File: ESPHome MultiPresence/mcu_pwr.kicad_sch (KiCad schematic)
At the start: 26 parts, among them J2 USB_C_Receptacle_Power

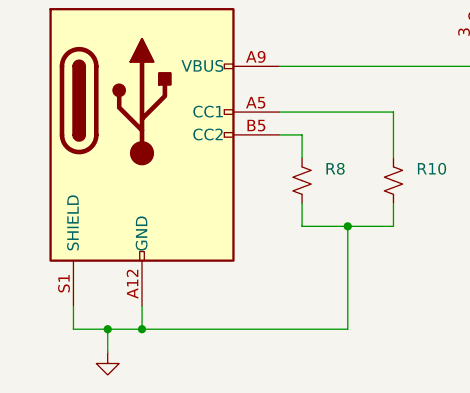
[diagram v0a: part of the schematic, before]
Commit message: small schematic changes
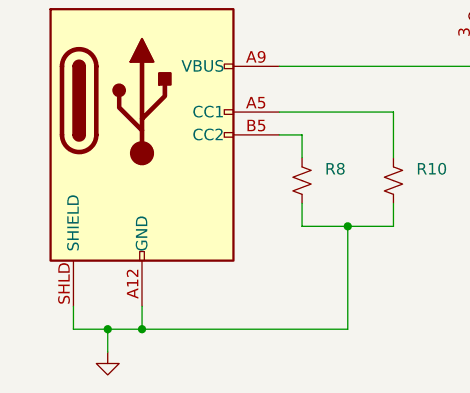
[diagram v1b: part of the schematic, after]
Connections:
- net GND: now also J2.SHLD (SHIELD); no longer J2.S1 (SHIELD)
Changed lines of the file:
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@@
     (pin "B5")
     (pin "B9")
-    (pin "S1")
+    (pin "SHLD")
   )
   (symbol (lib_id "Device:R_Small_US") (at 229.87 90.17 0) (unit 1)

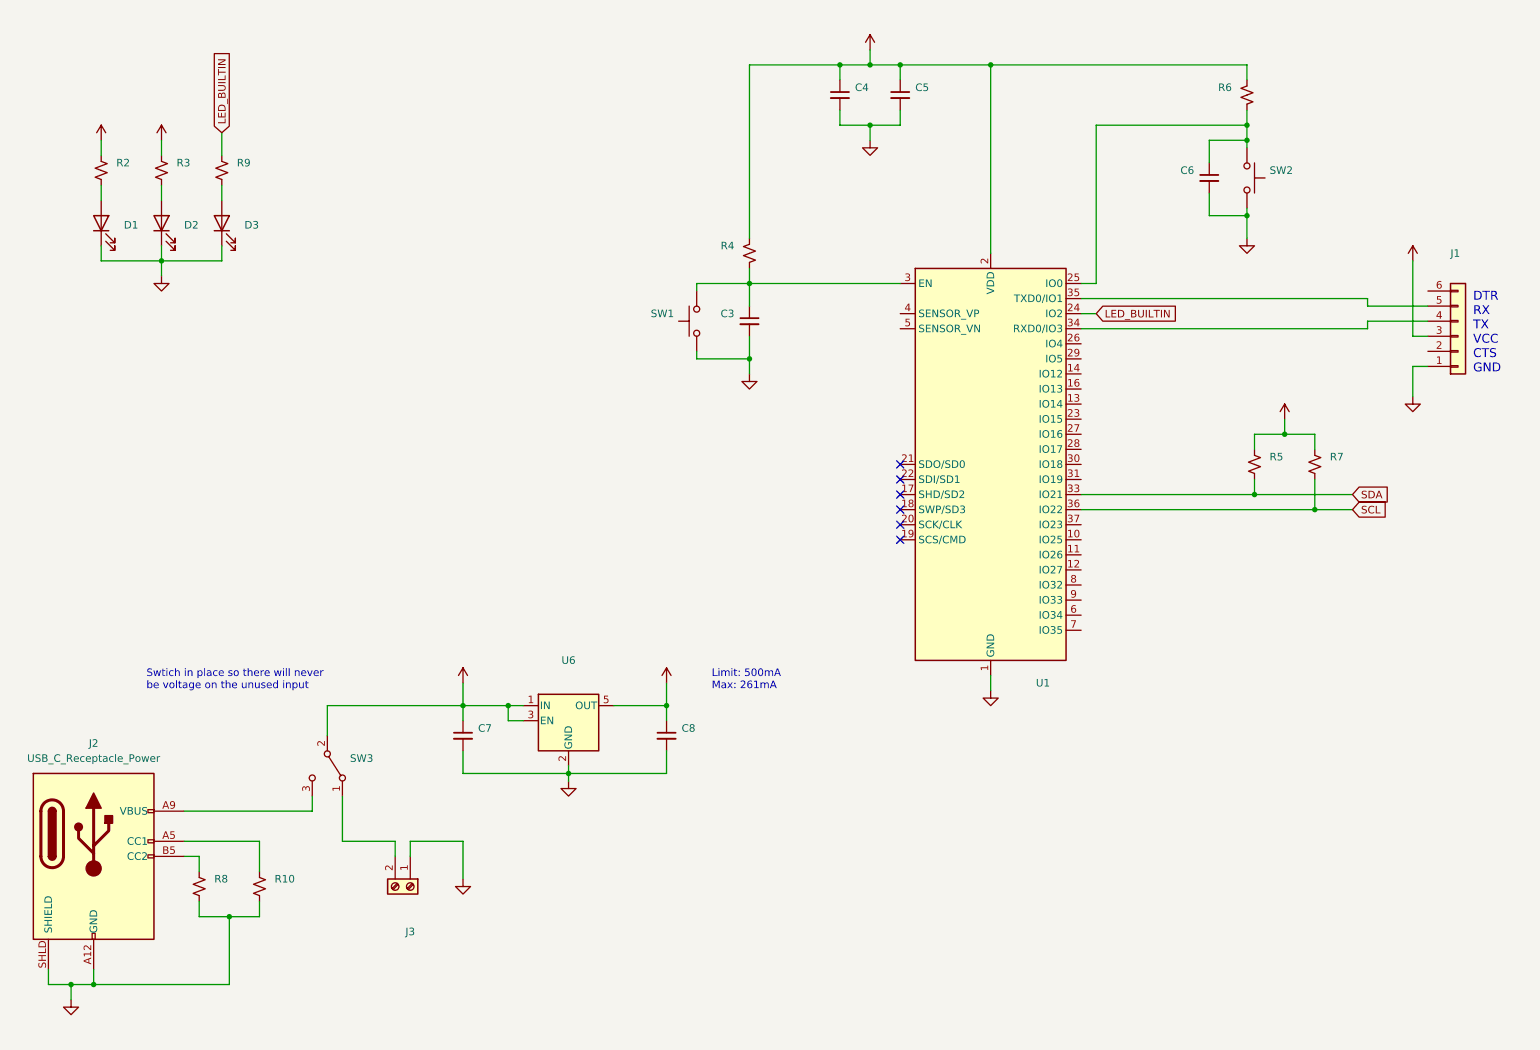
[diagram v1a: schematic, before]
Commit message: changed voltage switch to jumpper, changed screw terminal jst-ph
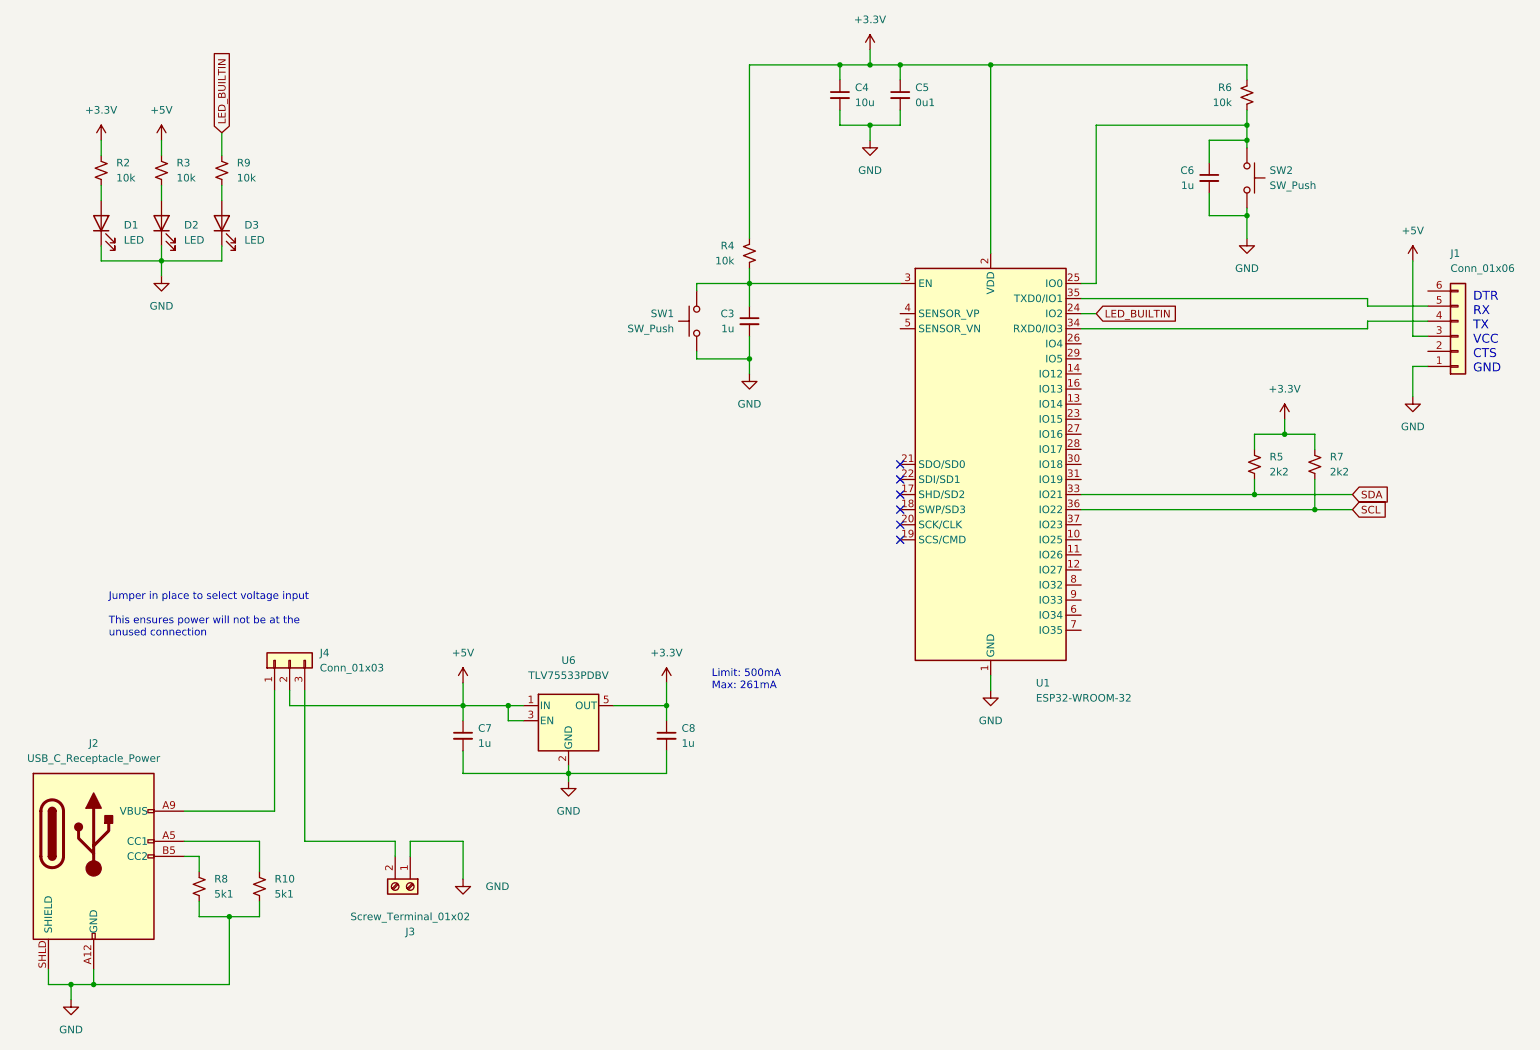
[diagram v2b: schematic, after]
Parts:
- removed SW3: (no value), symbol Switch:SW_SPDT
- added J4: Conn_01x03, Connector_PinHeader_2.54mm:PinHeader_1x03_P2.54mm_Vertical, symbol Connector_Generic:Conn_01x03
- C3, C6, C7, C8: value (none) -> 1u; footprint (none) -> Resistor_SMD:R_0603_1608Metric
- C4: value (none) -> 10u; footprint (none) -> Resistor_SMD:R_0603_1608Metric
- C5: value (none) -> 0u1; footprint (none) -> Resistor_SMD:R_0603_1608Metric
- D1, D2, D3: value (none) -> LED; footprint (none) -> Diode_SMD:D_0603_1608Metric
- J1: value (none) -> Conn_01x06; footprint (none) -> Connector_PinHeader_2.54mm:PinHeader_1x06_P2.54mm_Vertical
- J3: value (none) -> Screw_Terminal_01x02; footprint (none) -> Connector_JST:JST_PH_S2B-PH-K_1x02_P2.00mm_Horizontal
- R10, R8: value (none) -> 5k1; footprint (none) -> Resistor_SMD:R_0603_1608Metric
- R2, R3, R4, R6, R9: value (none) -> 10k; footprint (none) -> Resistor_SMD:R_0603_1608Metric
- R5, R7: value (none) -> 2k2; footprint (none) -> Resistor_SMD:R_0603_1608Metric
- SW1, SW2: value (none) -> SW_Push; footprint (none) -> Button_Switch_SMD:SW_SPST_EVQP2
- U1: value (none) -> ESP32-WROOM-32; footprint (none) -> RF_Module:ESP32-WROOM-32
- U6: value (none) -> TLV75533PDBV; footprint (none) -> Package_TO_SOT_SMD:SOT-23-5
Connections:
- net +5V: now also J4.2 (Pin_2)
- net at J3.2 (Pin_2): now also J4.3 (Pin_3)
- net at J2.A9 (VBUS), J2.B9 (VBUS): now also J4.1 (Pin_1)
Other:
- note added: "Jumper in place to select voltage input This ensures power will not be at the unused connection"
- note removed: "Swtich in place so there will never be voltage on the unused input"

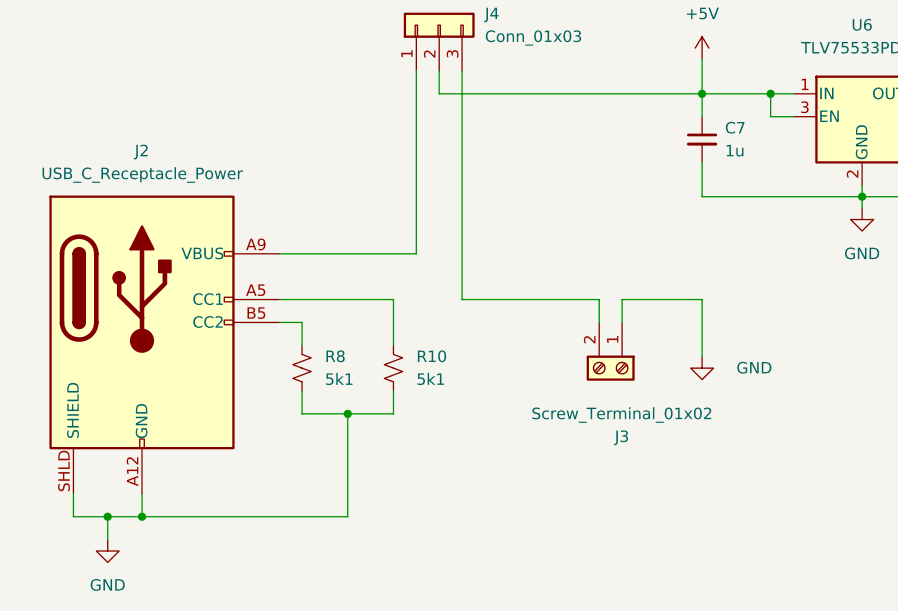
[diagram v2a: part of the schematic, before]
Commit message: replaced J3 with pinheadder, fixed USB-C footprint pin assignment
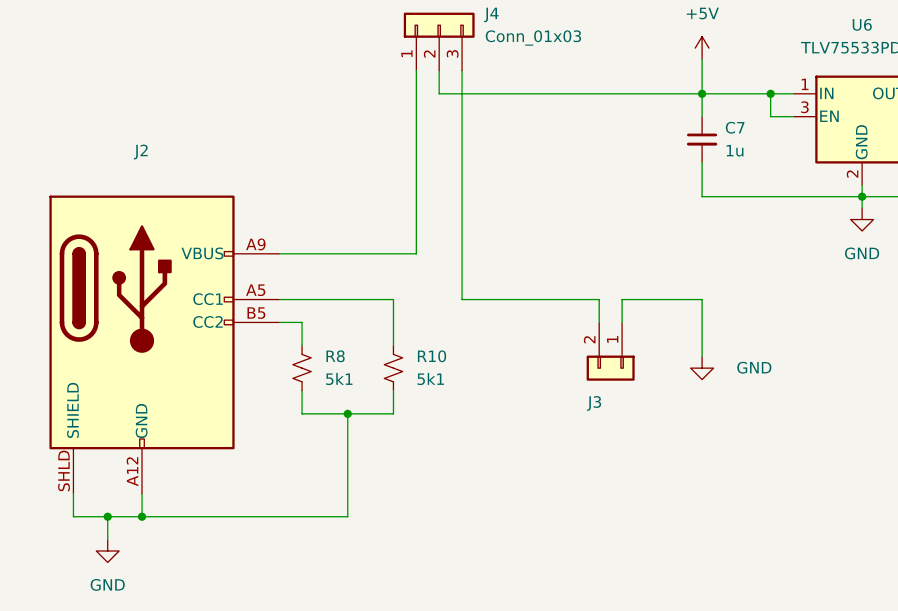
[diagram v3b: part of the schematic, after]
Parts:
- removed J3: Screw_Terminal_01x02, Connector_JST:JST_PH_S2B-PH-K_1x02_P2.00mm_Horizontal, symbol Connector:Screw_Terminal_01x02
- added J3: (no value), symbol Connector_Generic:Conn_01x02
- J2: value USB_C_Receptacle_Power -> (none); footprint My Footprints:USB_C_Power -> (none)
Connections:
- net GND: now also J3.1 (Pin_1)
- net at J4.3 (Pin_3): now also J3.2 (Pin_2)
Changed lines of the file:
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@@
     (pin "1")
-  )
-  (symbol (lib_id "Connector:Screw_Terminal_01x02") (at 87.63 161.29 270) (unit 1)
-    (in_bom yes) (on_board yes)
-    (property "Reference" "J3" (id 0) (at 87.63 168.91 90))
-    (property "Value" "Screw_Terminal_01x02" (id 1) (at 87.63 166.37 90))
-    (property "Footprint" "Connector_JST:JST_PH_S2B-PH-K_1x02_P2.00mm_Horizontal" (id 2) (at 87.63 161.29 0)
-      (effects (font (size 1.27 1.27)) hide)
-    )
-    (property "Datasheet" "~" (id 3) (at 87.63 161.29 0)
-      (effects (font (size 1.27 1.27)) hide)
-    )
-    (pin "1")
-    (pin "2")
   )
   (symbol (lib_id "power:GND") (at 45.72 58.42 0) (mirror y) (unit 1)
@@
     (pin "1")
   )
+  (symbol (lib_id "Connector_Generic:Conn_01x02") (at 87.63 161.29 270) (unit 1)
+    (in_bom yes) (on_board yes)
+    (property "Reference" "J3" (id 0) (at 83.82 165.1 90)
+      (effects (font (size 1.27 1.27)) (justify left))
+    )
+    (property "Value" "" (id 1) (at 83.82 167.64 90)
+      (effects (font (size 1.27 1.27)) (justify left))
+    )
+    (property "Footprint" "" (id 2) (at 87.63 161.29 0)
+      (effects (font (size 1.27 1.27)) hide)
+    )
+    (property "Datasheet" "~" (id 3) (at 87.63 161.29 0)
+      (effects (font (size 1.27 1.27)) hide)
+    )
+    (pin "1")
+    (pin "2")
+  )
   (symbol (lib_id "Device:C_Small") (at 160.02 27.94 0) (unit 1)
     (in_bom yes) (on_board yes) (fields_autoplaced)
@@
     (in_bom yes) (on_board yes) (fields_autoplaced)
     (property "Reference" "J2" (id 0) (at 34.29 137.16 0))
-    (property "Value" "USB_C_Receptacle_Power" (id 1) (at 34.29 139.7 0))
-    (property "Footprint" "My Footprints:USB_C_Power" (id 2) (at 38.1 152.4 0)
-      (effects (font (size 1.27 1.27)) hide)
-    )
+    (property "Value" "" (id 1) (at 34.29 139.7 0))
+    (property "Footprint" "" (id 2) (at 38.1 152.4 0)
+      (effects (font (size 1.27 1.27)) hide)
+    )
